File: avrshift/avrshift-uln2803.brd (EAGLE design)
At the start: 49.2 x 49.5 mm, 33 parts, among them IC1 AT90S2313P, IC2 7805TV, IC3 ULN2803A, IC4 ULN2803A

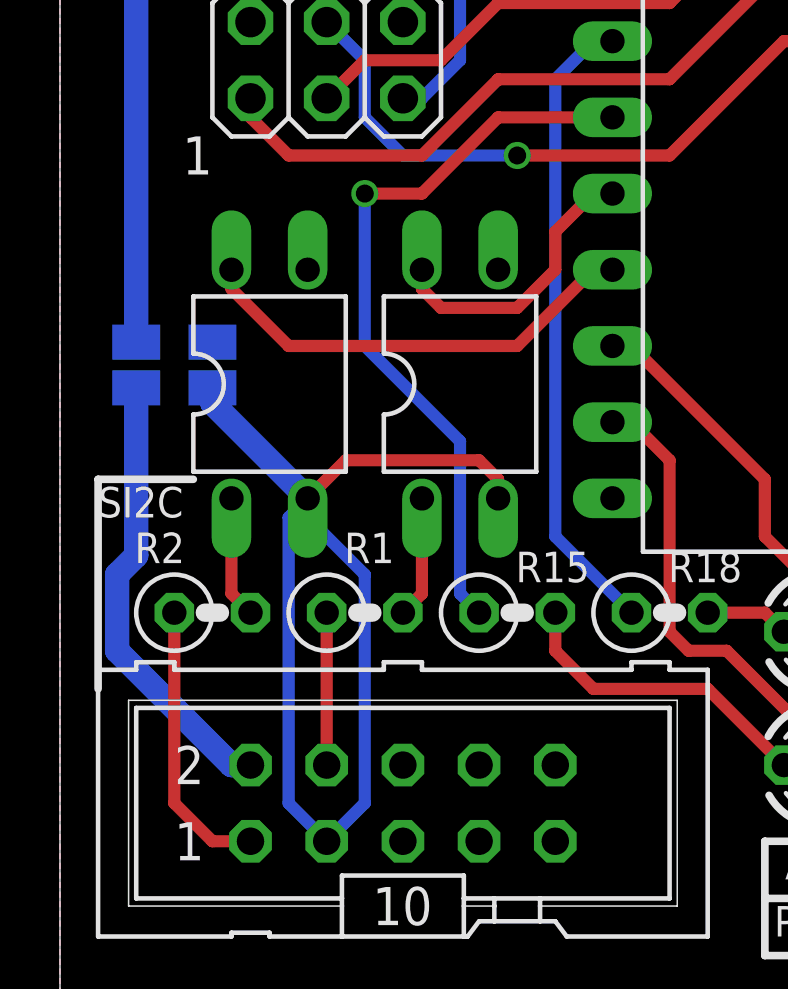
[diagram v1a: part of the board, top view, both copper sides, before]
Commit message: avrshift-uln: allow PC827 drop-in replacement here too
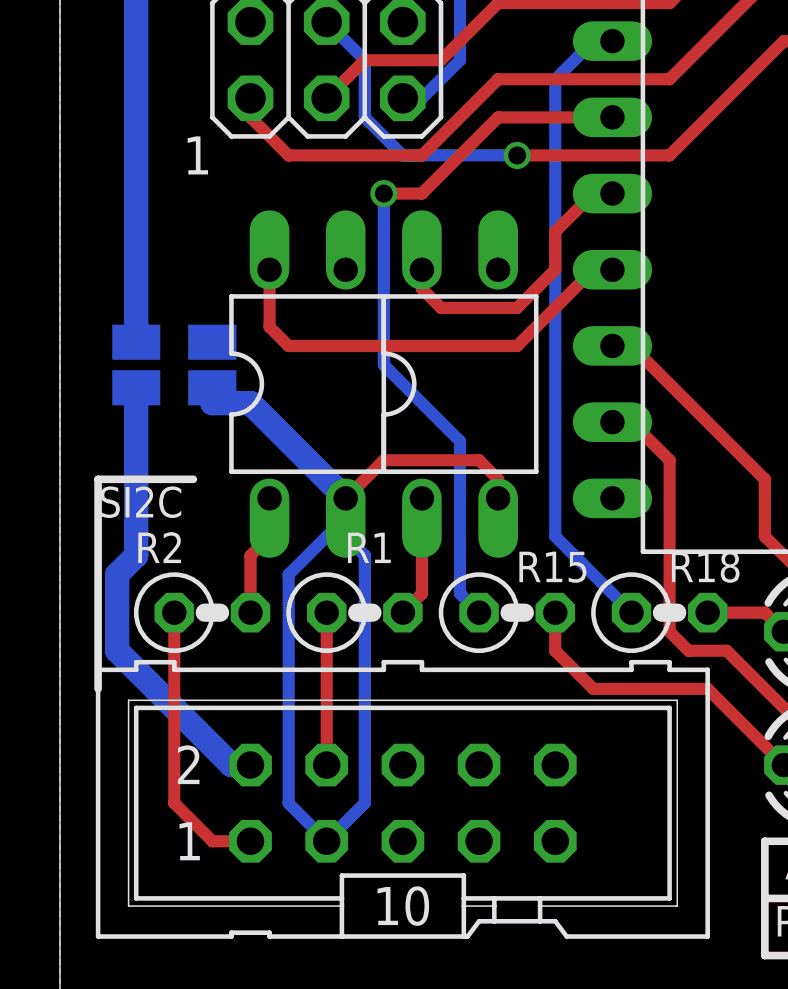
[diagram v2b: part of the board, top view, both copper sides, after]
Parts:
- moved OK2 1.27 mm to (8.26, 20.3)
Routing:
- net N$33: track 24.9 -> 24.0 mm
- net BUSGND: track 37.7 -> 37.1 mm
- net AVRSDA: track 15.2 -> 14.7 mm
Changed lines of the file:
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@@
 </class>
 </classes>
-<designrules name="dirtypcbs_v1">
+<designrules name="dirtypcbs_v1 *">
 <description language="en">&lt;b&gt;Dirty Cheap Dirty Board Design Rules&lt;/b&gt;
 &lt;br&gt;
@@
 <param name="dpGapFactor" value="2.5"/>
 <param name="checkGrid" value="0"/>
-<param name="checkAngle" value="0"/>
+<param name="checkAngle" value="1"/>
 <param name="checkFont" value="1"/>
-<param name="checkRestrict" value="0"/>
+<param name="checkRestrict" value="1"/>
 <param name="useDiameter" value="13"/>
 <param name="maxErrors" value="50"/>
@@
 <attribute name="NAME" x="14.732" y="18.669" size="1.27" layer="27" ratio="10" rot="R180"/>
 </element>
-<element name="OK2" library="optocoupler" package="DIL04" value="PC817" x="6.985" y="20.32" smashed="yes">
-<attribute name="OC_NEWARK" value="97K7059" x="34.925" y="12.7" size="1.778" layer="27" display="off"/>
-<attribute name="MPN" value="PC817X4J000F" x="34.925" y="12.7" size="1.778" layer="27" display="off"/>
-<attribute name="MF" value="" x="34.925" y="12.7" size="1.778" layer="27" display="off"/>
-<attribute name="OC_FARNELL" value="9707727" x="34.925" y="12.7" size="1.778" layer="27" display="off"/>
-<attribute name="VALUE" x="11.176" y="17.399" size="1.27" layer="27" ratio="10" rot="R90"/>
-<attribute name="NAME" x="8.382" y="18.669" size="1.27" layer="27" ratio="10" rot="R180"/>
+<element name="OK2" library="optocoupler" package="DIL04" value="PC817" x="8.255" y="20.32" smashed="yes">
+<attribute name="OC_NEWARK" value="97K7059" x="36.195" y="12.7" size="1.778" layer="27" display="off"/>
+<attribute name="MPN" value="PC817X4J000F" x="36.195" y="12.7" size="1.778" layer="27" display="off"/>
+<attribute name="MF" value="" x="36.195" y="12.7" size="1.778" layer="27" display="off"/>
+<attribute name="OC_FARNELL" value="9707727" x="36.195" y="12.7" size="1.778" layer="27" display="off"/>
+<attribute name="VALUE" x="12.446" y="17.399" size="1.27" layer="27" ratio="10" rot="R90"/>
+<attribute name="NAME" x="9.652" y="18.669" size="1.27" layer="27" ratio="10" rot="R180"/>
 </element>
 <element name="IC2" library="linear" package="TO220V" value="7805TV" x="13.97" y="43.18" smashed="yes" rot="R270">
@@
 <contactref element="OK2" pad="1"/>
 <contactref element="R2" pad="2"/>
-<wire x1="6.35" y1="12.7" x2="5.715" y2="13.335" width="0.4064" layer="1"/>
-<wire x1="5.715" y1="13.335" x2="5.715" y2="16.51" width="0.4064" layer="1"/>
+<wire x1="6.985" y1="16.51" x2="6.985" y2="15.24" width="0.4064" layer="1"/>
+<wire x1="6.985" y1="15.24" x2="6.35" y2="14.605" width="0.4064" layer="1"/>
+<wire x1="6.35" y1="14.605" x2="6.35" y2="12.7" width="0.4064" layer="1"/>
 </signal>
 <signal name="SCL">
@@
 <wire x1="14.605" y1="16.51" x2="14.605" y2="17.145" width="0.4064" layer="1"/>
 <wire x1="14.605" y1="17.145" x2="13.97" y2="17.78" width="0.4064" layer="1"/>
-<wire x1="13.97" y1="17.78" x2="9.525" y2="17.78" width="0.4064" layer="1"/>
-<wire x1="9.525" y1="17.78" x2="8.255" y2="16.51" width="0.4064" layer="1"/>
+<wire x1="13.97" y1="17.78" x2="10.795" y2="17.78" width="0.4064" layer="1"/>
+<wire x1="10.795" y1="17.78" x2="9.525" y2="16.51" width="0.4064" layer="1"/>
 <wire x1="5.08" y1="20.193" x2="5.08" y2="19.685" width="0.8128" layer="16"/>
-<wire x1="5.08" y1="19.685" x2="8.255" y2="16.51" width="0.8128" layer="16"/>
 <wire x1="8.89" y1="5.08" x2="7.62" y2="6.35" width="0.4064" layer="16"/>
-<wire x1="7.62" y1="6.35" x2="7.62" y2="15.875" width="0.4064" layer="16"/>
-<wire x1="7.62" y1="15.875" x2="8.255" y2="16.51" width="0.4064" layer="16"/>
+<wire x1="7.62" y1="6.35" x2="7.62" y2="13.97" width="0.4064" layer="16"/>
 <wire x1="8.89" y1="5.08" x2="10.16" y2="6.35" width="0.4064" layer="16"/>
-<wire x1="10.16" y1="6.35" x2="10.16" y2="13.97" width="0.4064" layer="16"/>
-<wire x1="10.16" y1="13.97" x2="8.255" y2="15.875" width="0.4064" layer="16"/>
-<wire x1="8.255" y1="15.875" x2="8.255" y2="16.51" width="0.4064" layer="16"/>
+<wire x1="10.16" y1="6.35" x2="10.16" y2="14.605" width="0.4064" layer="16"/>
+<wire x1="10.16" y1="14.605" x2="9.525" y2="15.24" width="0.4064" layer="16"/>
+<wire x1="9.525" y1="15.24" x2="9.525" y2="15.875" width="0.4064" layer="16"/>
+<wire x1="7.62" y1="13.97" x2="9.525" y2="15.875" width="0.4064" layer="16"/>
+<wire x1="9.525" y1="15.875" x2="9.525" y2="16.51" width="0.4064" layer="16"/>
+<wire x1="5.08" y1="19.685" x2="6.35" y2="19.685" width="0.8128" layer="16"/>
+<wire x1="6.35" y1="19.685" x2="9.525" y2="16.51" width="0.8128" layer="16"/>
 </signal>
 <signal name="AVRSCL">
@@
 <contactref element="OK2" pad="4"/>
 <contactref element="IC1" pad="7"/>
-<wire x1="5.715" y1="24.13" x2="5.715" y2="23.495" width="0.4064" layer="1"/>
-<wire x1="5.715" y1="23.495" x2="7.62" y2="21.59" width="0.4064" layer="1"/>
-<wire x1="7.62" y1="21.59" x2="15.24" y2="21.59" width="0.4064" layer="1"/>
 <wire x1="15.24" y1="21.59" x2="17.78" y2="24.13" width="0.4064" layer="1"/>
 <wire x1="17.78" y1="24.13" x2="18.415" y2="24.13" width="0.4064" layer="1"/>
+<wire x1="6.985" y1="24.13" x2="6.985" y2="22.225" width="0.4064" layer="1"/>
+<wire x1="6.985" y1="22.225" x2="7.62" y2="21.59" width="0.4064" layer="1"/>
+<wire x1="7.62" y1="21.59" x2="15.24" y2="21.59" width="0.4064" layer="1"/>
 </signal>
 <signal name="BUSVCC">
@@
 <wire x1="18.415" y1="29.21" x2="14.605" y2="29.21" width="0.4064" layer="1"/>
 <wire x1="14.605" y1="29.21" x2="12.065" y2="26.67" width="0.4064" layer="1"/>
-<wire x1="12.065" y1="26.67" x2="10.16" y2="26.67" width="0.4064" layer="1"/>
-<via x="10.16" y="26.67" extent="1-16" drill="0.6"/>
-<wire x1="10.16" y1="26.67" x2="10.16" y2="21.59" width="0.4064" layer="16"/>
-<wire x1="10.16" y1="21.59" x2="13.335" y2="18.415" width="0.4064" layer="16"/>
+<wire x1="12.065" y1="26.67" x2="10.795" y2="26.67" width="0.4064" layer="1"/>
+<via x="10.795" y="26.67" extent="1-16" drill="0.6"/>
+<wire x1="10.795" y1="26.67" x2="10.795" y2="20.955" width="0.4064" layer="16"/>
+<wire x1="10.795" y1="20.955" x2="13.335" y2="18.415" width="0.4064" layer="16"/>
 <wire x1="13.335" y1="18.415" x2="13.335" y2="13.335" width="0.4064" layer="16"/>
 <contactref element="R15" pad="1"/>

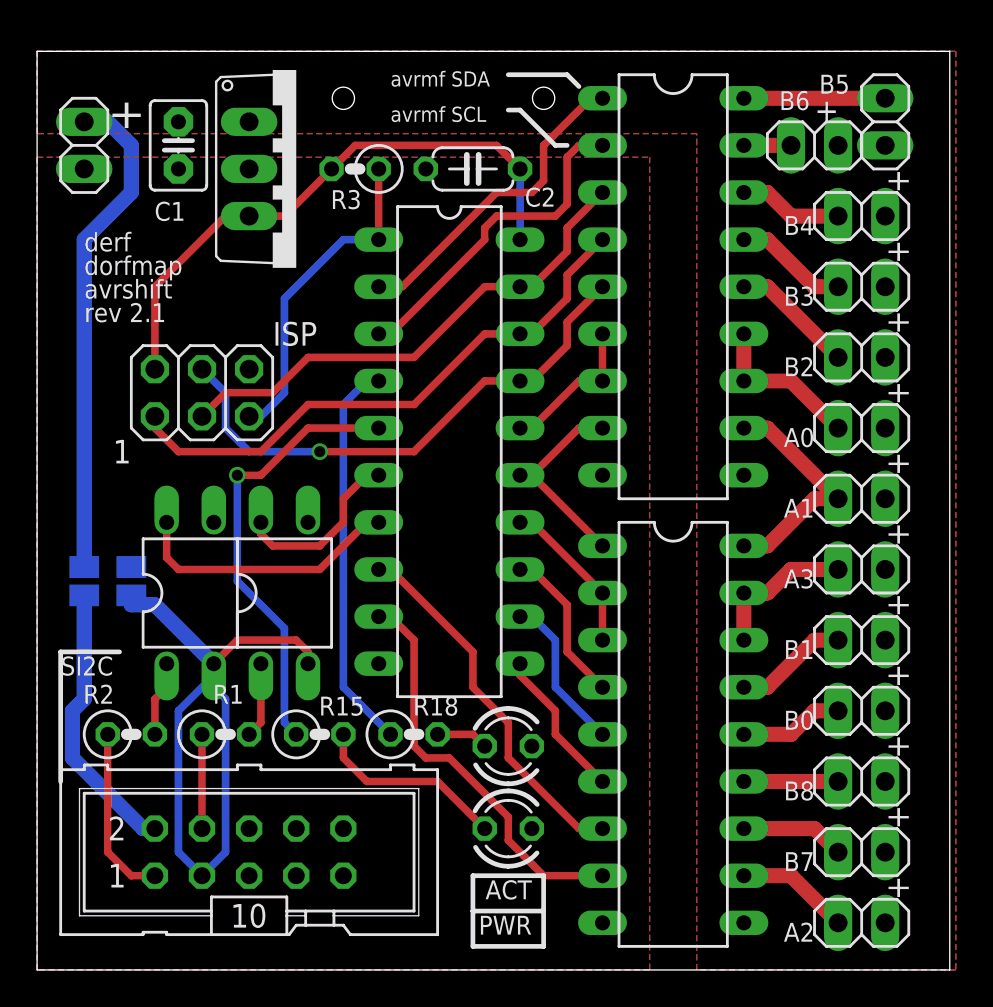
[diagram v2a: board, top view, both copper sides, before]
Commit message: avrshift-uln2803: switch to (cheaper) SMD ATTiny
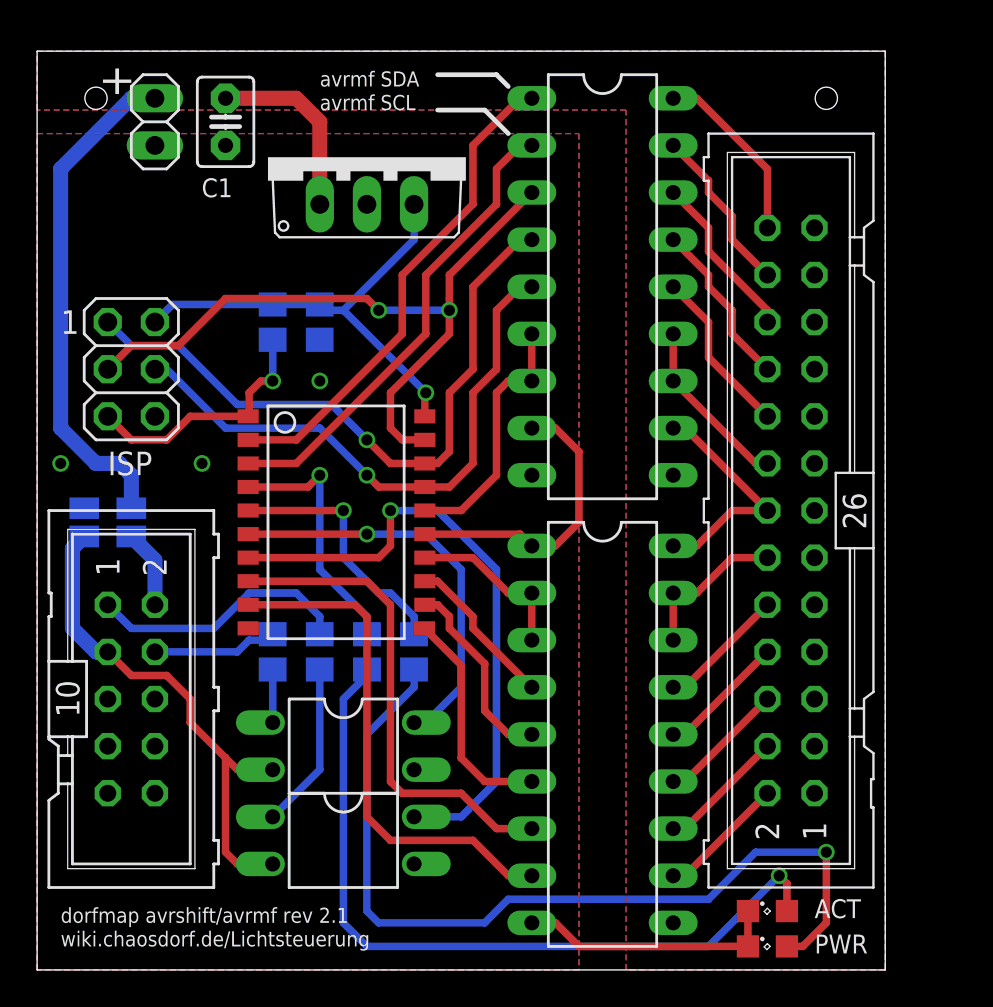
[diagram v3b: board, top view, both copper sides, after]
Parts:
- removed JP10, JP11, JP12, JP13, JP14, JP2, JP3, JP4, JP5, JP6, JP7, JP8, JP9: (no value), pinhead:1X02
- removed R15, R18: 470, rcl:0207/2V
- added R4, R5: 470, rcl:R0805
- added SV3: (no value), con-ml:ML26
- C2: device rcl:C050-024X044 -> rcl:C0805
- IC1: value AT90S2313P -> AT90S2313S; device atmel:DIL20 -> atmel:SO20L
- LED1, LED2: device led:LED3MM -> led:SML0805
- R1, R2, R3: device rcl:0207/2V -> rcl:R0805
- moved LED2 16.6 mm to (39.4, 3.17)
- moved OK2 15.7 mm to (16.5, 6.99), turned to 270 degrees
- moved LED1 15.3 mm to (39.4, 1.27)
- moved C2 11.7 mm to (15.2, 34.9), flipped to the bottom, turned to 270 degrees
- moved R2 11.1 mm to (15.2, 17.1), flipped to the bottom, turned to 270 degrees
- moved SV1 10.4 mm to (5.08, 14.6), turned to 270 degrees
- moved R3 9.38 mm to (12.7, 34.9), flipped to the bottom, turned to 90 degrees
- moved OK1 8.84 mm to (16.5, 12.1), turned to 270 degrees
- moved IC1 6.54 mm to (16.5, 24.8)
- moved R1 5.12 mm to (12.7, 17.1), flipped to the bottom, turned to 270 degrees
- moved SJ1 4.07 mm to (5.08, 24.1)
- moved SJ2 4.07 mm to (2.54, 24.1)
- moved SV2 4.02 mm to (5.08, 32.4), turned to 270 degrees
- moved JP1 4.02 mm to (6.35, 45.7)
- moved IC2 3.86 mm to (17.8, 43.8), turned to 0 degrees
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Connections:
- net GND: now also LED1.C, LED2.C; no longer LED1.K, LED2.K
- net N$10: now also R4.2; no longer R15.2
- net N$11: now also SV3.10; no longer JP10.1
- net N$12: now also SV3.12; no longer JP9.1
- net N$13: now also SV3.14; no longer JP8.1
- net N$14: now also SV3.16; no longer JP7.1
- net N$15: now also SV3.18; no longer JP6.1
- net N$17: now also SV3.4; no longer JP13.1
- net N$18: now also SV3.2; no longer JP14.1
- net N$2: now also SV3.26; no longer JP2.1
- net N$21: now also R5.1; no longer R18.1
- net N$25: now also SV3.20; no longer JP5.1
- net N$33: now also R4.1; no longer R15.1
- net N$5: now also SV3.24; no longer JP3.1
- net N$6: now also SV3.22; no longer JP4.1
- net N$7: now also SV3.8; no longer JP11.1
- net N$8: now also R5.2; no longer R18.2
- net N$9: now also SV3.6; no longer JP12.1
- net VCC: now also SV3.1, SV3.11, SV3.13, SV3.15, SV3.17, SV3.19, SV3.21, SV3.23, SV3.25, SV3.3, SV3.5, SV3.7, SV3.9; no longer JP10.2, JP11.2, JP12.2, JP13.2, JP14.2, JP2.2, JP3.2, JP4.2, JP5.2, JP6.2, JP7.2, JP8.2, JP9.2
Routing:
- net N$8: track 2.80 -> 41.9 mm, vias 0 -> 1
- net N$10: track 10.5 -> 47.1 mm, vias 0 -> 1
- net AVRSDA: track 14.7 -> 33.5 mm, vias 0 -> 1
- net GND: track 0.00 -> 14.3 mm, vias 0 -> 3
- net AVRSCL: track 9.57 -> 21.9 mm, vias 0 -> 1
- net AVRO13: track 27.3 -> 38.2 mm, vias 0 -> 2
- net BUSVCC: track 15.0 -> 4.21 mm
- net VCC: track 26.9 -> 37.3 mm
- net N$33: track 24.0 -> 13.8 mm
- net BUSGND: track 37.1 -> 27.8 mm
- net AVRO01: track 17.4 -> 26.6 mm
- net N$21: track 21.3 -> 13.8 mm, vias 0 -> 1
- net AVRO02: track 18.1 -> 25.4 mm
- net N$5: track 2.54 -> 9.09 mm
- net AVRO03: track 20.1 -> 26.4 mm
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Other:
- board size 49.2 x 49.5 mm -> 45.7 x 49.5 mm
- board text added: "dorfmap avrshift/avrmf rev 2.1"
- board text added: "wiki.chaosdorf.de/Lichtsteuerung"
- board text removed: "A0"
- board text removed: "A1"
- board text removed: "A2"
- board text removed: "A3"
- board text removed: "B0"
- board text removed: "B1"
- board text removed: "B2"
- board text removed: "B3"
- board text removed: "B4"
- board text removed: "B5"
- board text removed: "B6"
- board text removed: "B7"
- board text removed: "B8"
- board text removed: "SI2C"
- board text removed: "avrshift"
- board text removed: "derf"
- board text removed: "dorfmap"
- board text removed: "rev 2.1"
